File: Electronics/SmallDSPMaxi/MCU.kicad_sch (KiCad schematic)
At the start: 22 parts, among them J35 Header, SW5 TS-1187A-B-A-B, U46 STM32F030C8Tx, Y2 8MHz

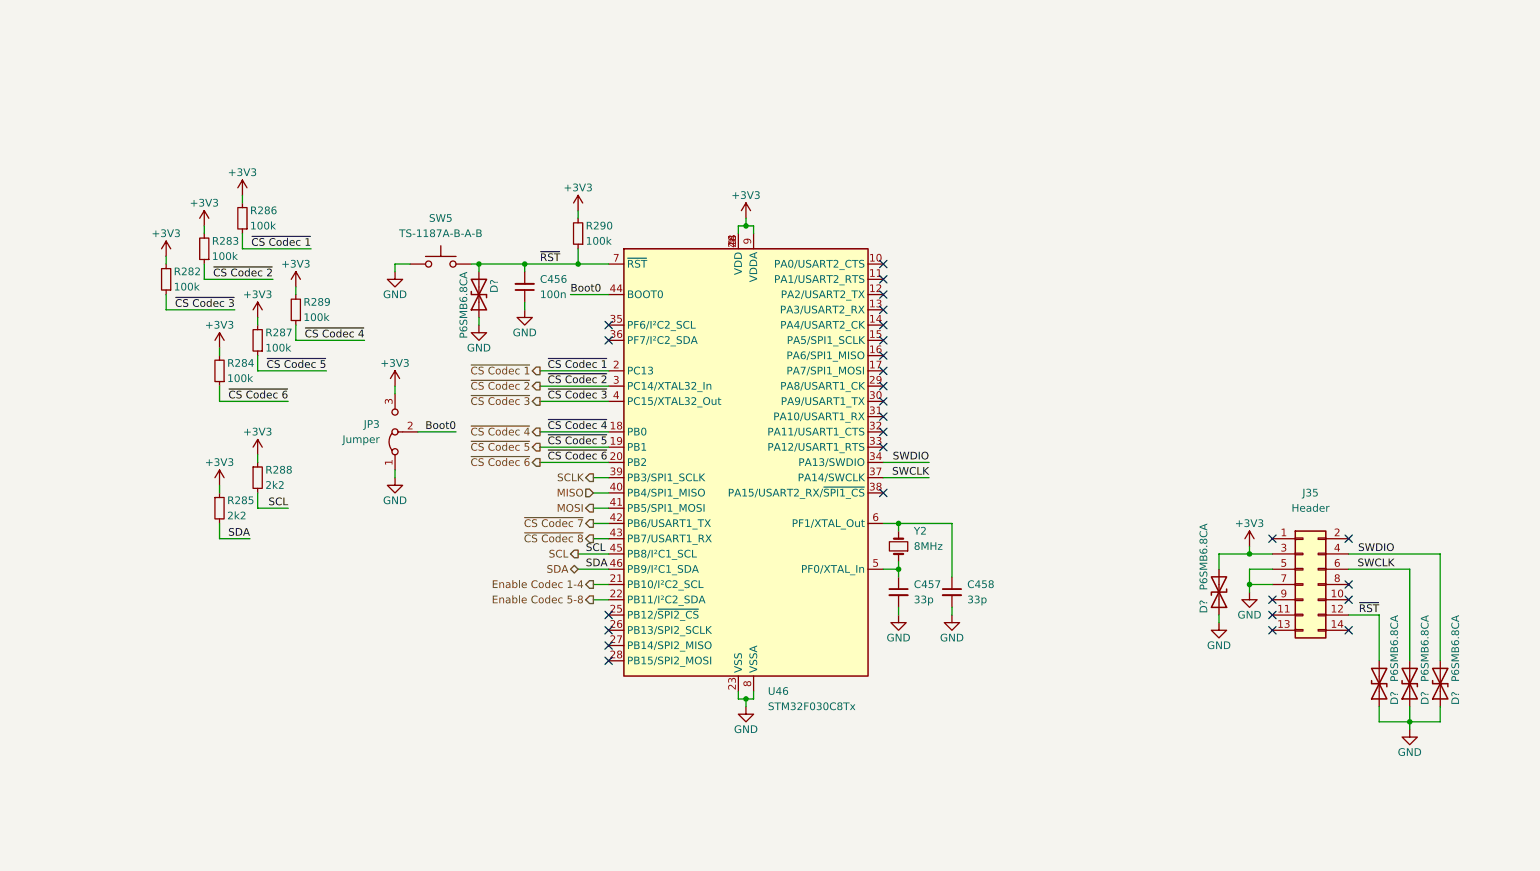
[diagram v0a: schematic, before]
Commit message: Finishes SmallDSP Maxi plus the fitting In- and Output Boards
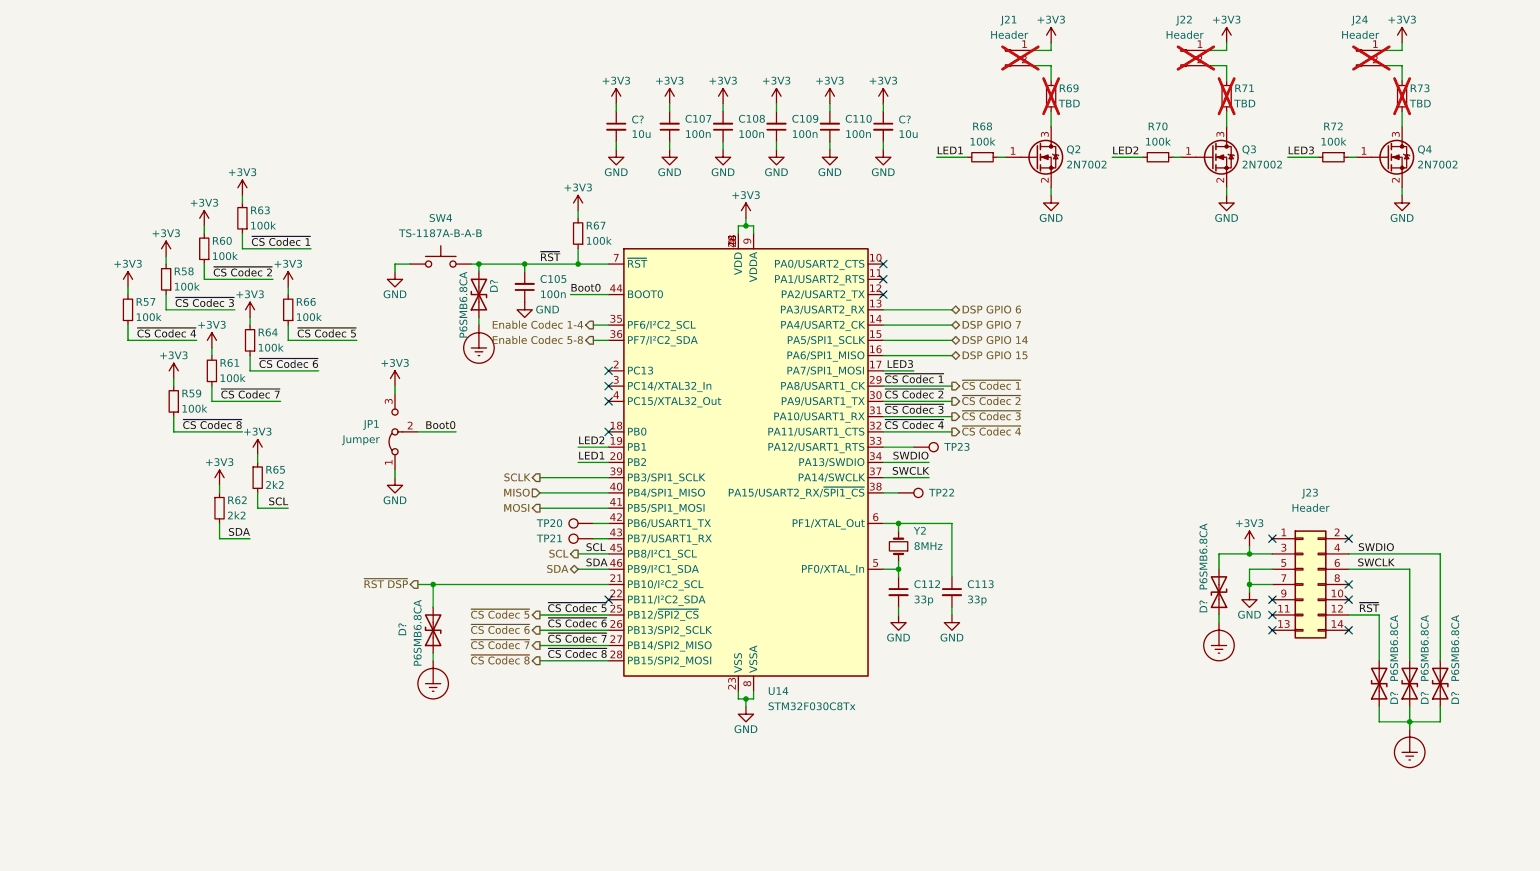
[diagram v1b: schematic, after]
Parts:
- added C107, C108, C109, C110: 100n, Capacitor_SMD:C_0402_1005Metric, symbol Device:C_Small
- added C? (x2): 10u, Capacitor_SMD:C_0603_1608Metric, symbol Device:C_Small
- added D?: P6SMB6.8CA, Diode_SMD:D_SMB, symbol Device:D_TVS
- added J21, J22, J24: Header, Connector_PinHeader_1.27mm:PinHeader_1x02_P1.27mm_Vertical, symbol Connector:Conn_01x02_Pin
- added Q2, Q3, Q4: 2N7002, Package_TO_SOT_SMD:SOT-23, symbol Device:Q_NMOS_GSD
- added R59, R61, R68, R70, R72: 100k, Resistor_SMD:R_0402_1005Metric, symbol Device:R_Small
- added R69, R71, R73: TBD, Resistor_SMD:R_0805_2012Metric_Pad1.20x1.40mm_HandSolder, symbol Device:R_Small
- added TP20, TP21, TP22, TP23: TestPoint, TestPoint:TestPoint_Pad_D1.0mm, symbol Connector:TestPoint
- C105: renamed from C456; JLC Part Number C307331 -> (none); LCSC Part # (none) -> C307331
- C112: renamed from C457; JLC Part Number C1562 -> (none); LCSC Part # (none) -> C1562
- C113: renamed from C458; JLC Part Number C1562 -> (none); LCSC Part # (none) -> C1562
- D? (x5): JLC Part Number C78395 -> (none); LCSC Part # (none) -> C78395
- J23: renamed from J35; LCSC Part # (none) -> -
- JP1: renamed from JP3; LCSC Part # (none) -> -; Manufacturer (none) -> -; Part Number (none) -> -
- R57: renamed from R289; JLC Part Number C25741 -> (none); LCSC Part # (none) -> C25741
- R58: renamed from R282; JLC Part Number C25741 -> (none); LCSC Part # (none) -> C25741
- R60: renamed from R283; JLC Part Number C25741 -> (none); LCSC Part # (none) -> C25741
- R62: renamed from R285; JLC Part Number C25879 -> (none); LCSC Part # (none) -> C25879
- R63: renamed from R286; JLC Part Number C25741 -> (none); LCSC Part # (none) -> C25741
- R64: renamed from R284; JLC Part Number C25741 -> (none); LCSC Part # (none) -> C25741
- R65: renamed from R288; JLC Part Number C25879 -> (none); LCSC Part # (none) -> C25879
- R66: renamed from R287; JLC Part Number C25741 -> (none); LCSC Part # (none) -> C25741
- R67: renamed from R290; JLC Part Number C25741 -> (none); LCSC Part # (none) -> C25741
- SW4: renamed from SW5; JLC Part Number C318884 -> (none); LCSC Part # (none) -> C318884
- U14: renamed from U46; JLC Part Number C23922 -> (none); LCSC Part # (none) -> C23922
- Y2: JLC Part Number C115962 -> (none); LCSC Part # (none) -> C115962
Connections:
- net +3V3: now also C107.2, C108.2, C109.2, C110.2, C?.1, C?.1, J21.1 (Pin_1), J22.1 (Pin_1), J24.1 (Pin_1), R59.2, R61.2
- net Enable Codec 1-4: now also U14.35 (PF6/I²C2_SCL); no longer U14.21 (PB10/I²C2_SCL)
- net Enable Codec 5-8: now also U14.36 (PF7/I²C2_SDA); no longer U14.22 (PB11/I²C2_SDA)
- net GND: now also C107.1, C108.1, C109.1, C110.1, C?.2, C?.2, Q2.2 (S), Q3.2 (S), Q4.2 (S); no longer D?.1 (A1), D?.1 (A1), D?.1 (A1), D?.1 (A1), D?.1 (A1)
- net ~{CS Codec 1}: now also U14.29 (PA8/USART1_CK); no longer U14.2 (PC13)
- net ~{CS Codec 2}: now also U14.30 (PA9/USART1_TX); no longer U14.3 (PC14/XTAL32_In)
- net ~{CS Codec 3}: now also U14.31 (PA10/USART1_RX); no longer U14.4 (PC15/XTAL32_Out)
- net ~{CS Codec 4}: now also U14.32 (PA11/USART1_CTS); no longer U14.18 (PB0)
- net ~{CS Codec 5}: now also U14.25 (PB12/~{SPI2_CS}); no longer U14.19 (PB1)
- net ~{CS Codec 6}: now also U14.26 (PB13/SPI2_SCLK); no longer U14.20 (PB2)
- net ~{CS Codec 7}: now also U14.27 (PB14/SPI2_MISO), R61.1; no longer U14.42 (PB6/USART1_TX)
- net ~{CS Codec 8}: now also U14.28 (PB15/SPI2_MOSI), R59.1; no longer U14.43 (PB7/USART1_RX)
- net DSP GPIO 6: now reaches U14.13 (PA3/USART2_RX)
- net DSP GPIO 7: now reaches U14.14 (PA4/USART2_CK)
- net DSP GPIO 14: now reaches U14.15 (PA5/SPI1_SCLK)
- net DSP GPIO 15: now reaches U14.16 (PA6/SPI1_MISO)
- net LED3: now reaches U14.17 (PA7/SPI1_MOSI)
- net LED3: now also R72.2
- net at U14.33 (PA12/USART1_RTS): now also TP23.1
- net at U14.38 (PA15/USART2_RX/~{SPI1_CS}): now also TP22.1
- new net: Q2.1 (G), R68.1
- new net: J21.2 (Pin_2), R69.1
- new net: Q3.1 (G), R70.1
- new net: TP20.1, U14.42 (PB6/USART1_TX)
- new net: TP21.1, U14.43 (PB7/USART1_RX)
- new net: J24.2 (Pin_2), R73.1
- new net: J22.2 (Pin_2), R71.1
- new net: Q4.3 (D), R73.2
- new net: Q4.1 (G), R72.1
- new net: Q2.3 (D), R69.2
- new net: Q3.3 (D), R71.2
- new net Earth_Protective: D?.1 (A1), D?.1 (A1), D?.1 (A1), D?.1 (A1), D?.1 (A1), D?.1 (A1)
- new net LED1: R68.2, U14.20 (PB2)
- new net LED2: R70.2, U14.19 (PB1)
- new net ~{RST DSP}: D?.2 (A2), U14.21 (PB10/I²C2_SCL)
- no-connect marks 28 -> 16
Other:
- moved on the sheet: R57, R64, R66

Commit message: replaces 12pin IDC out header with 14pin one because of better availability.
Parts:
- J23: footprint Connector_PinHeader_1.27mm:PinHeader_2x07_P1.27mm_Vertical_SMD -> Connector_PinHeader_1.27mm:PinHeader_2x07_P1.27mm_Vertical; Part Number 20021121-00014T4LF -> 20021111-00014T1LF

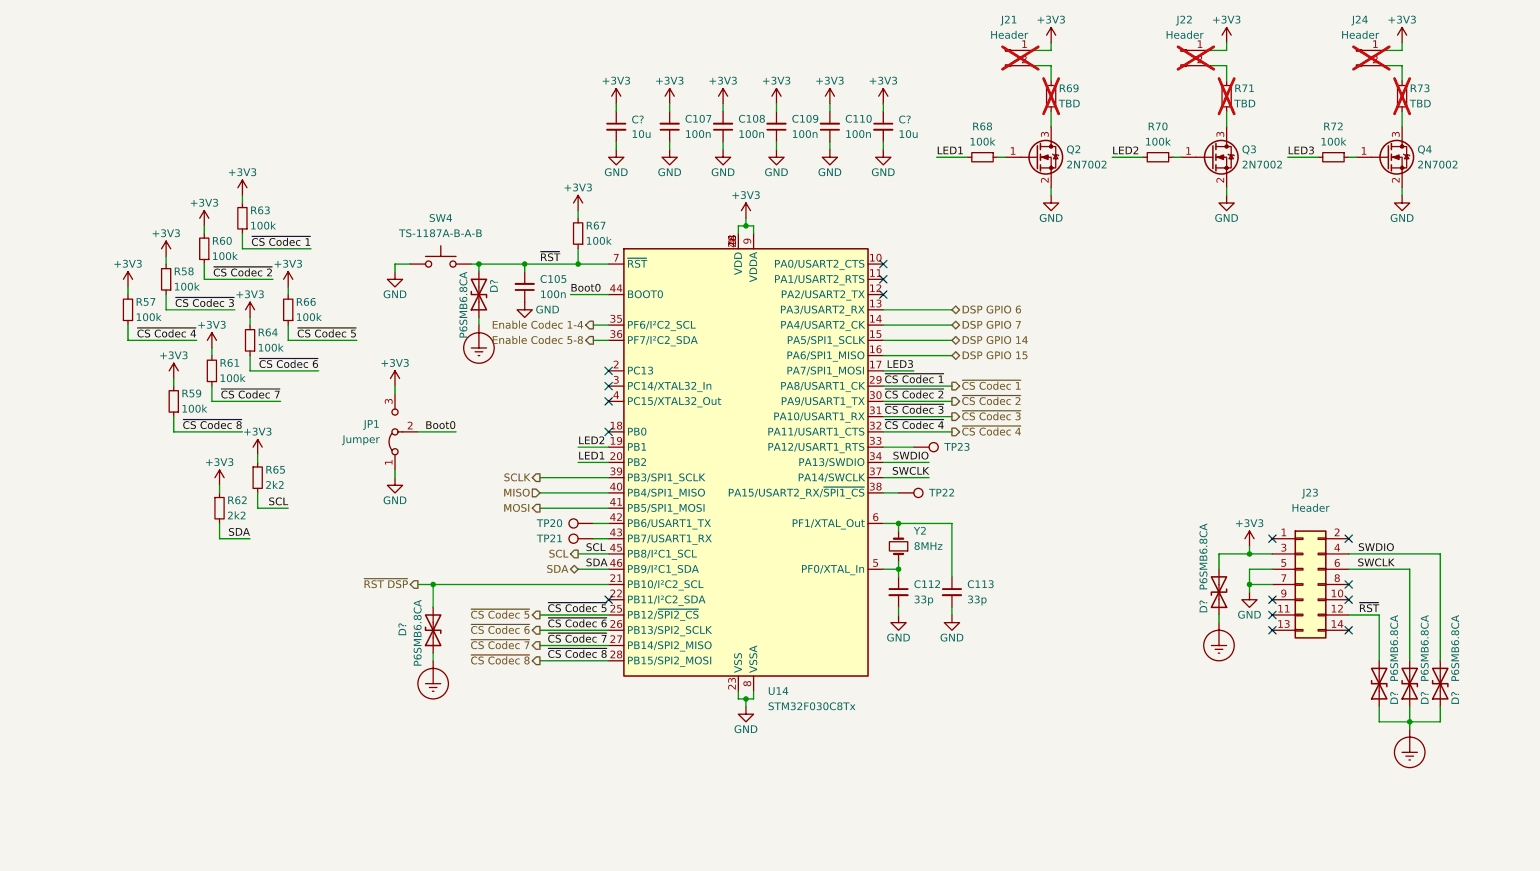
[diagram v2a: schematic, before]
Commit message: Fixes schematic mistakes, like incorrect routin of clock to codecs
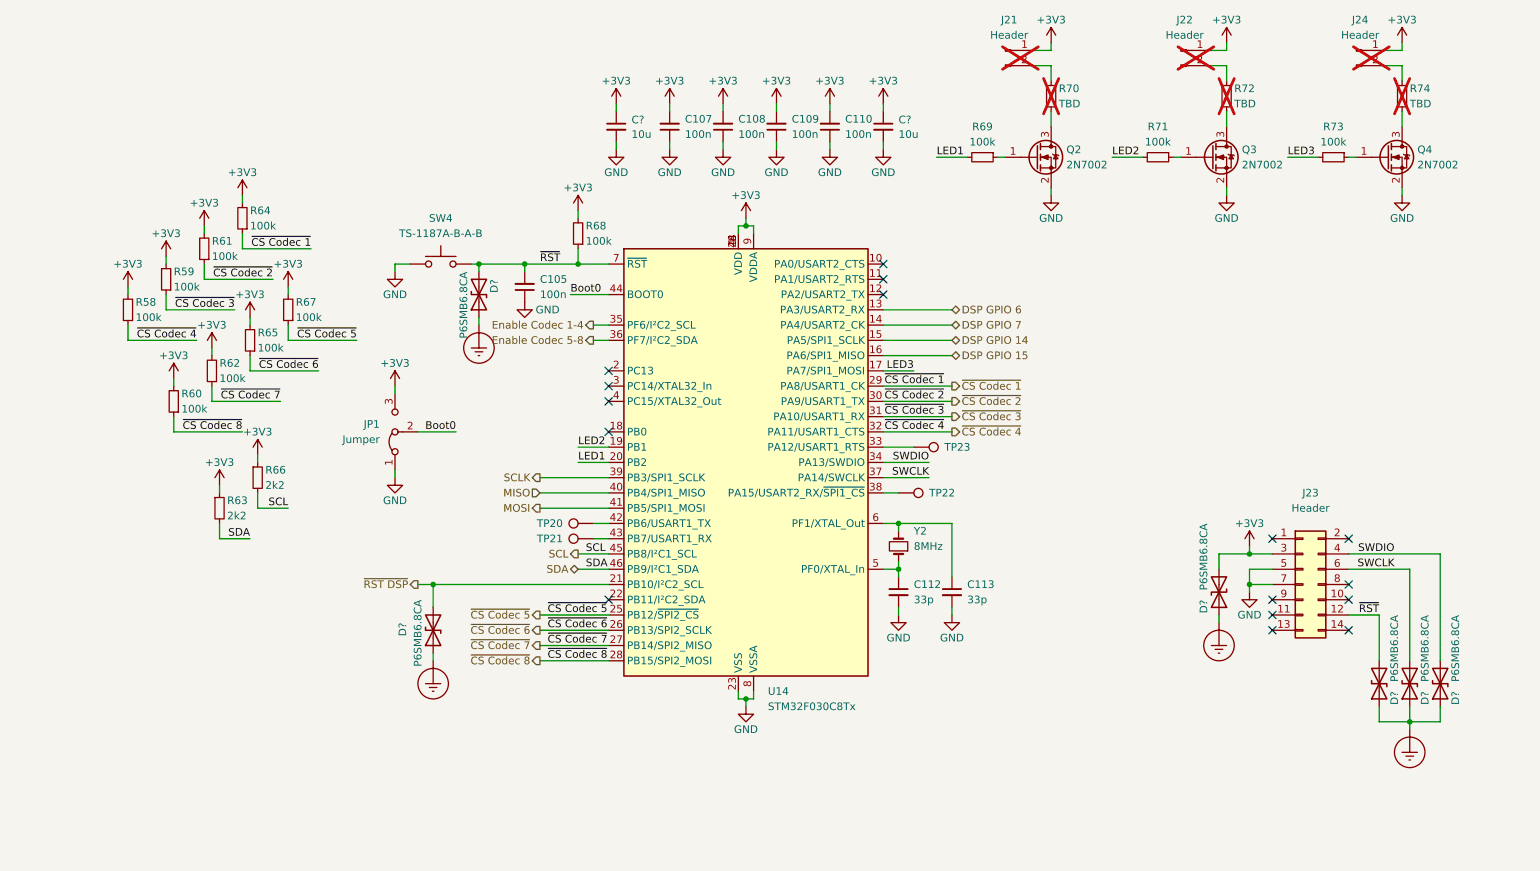
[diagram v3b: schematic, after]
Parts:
- renumbered R57 to R58, R58 to R59, R59 to R60, R60 to R61, R61 to R62, R62 to R63, R63 to R64, R64 to R65, R65 to R66, R66 to R67, R67 to R68, R68 to R69, R69 to R70, R70 to R71, R71 to R72, R72 to R73, R73 to R74

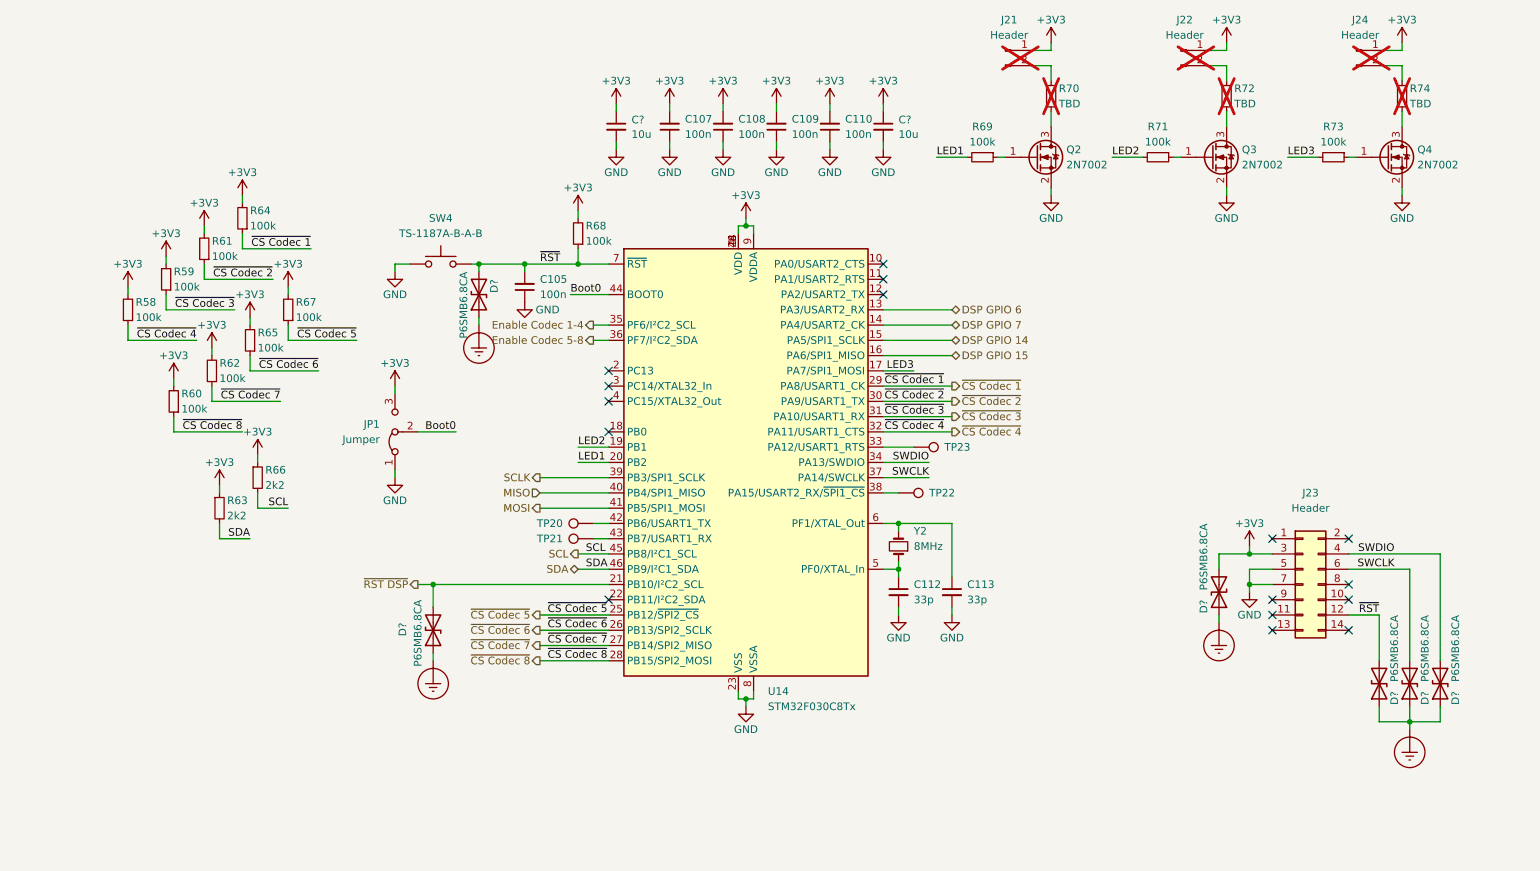
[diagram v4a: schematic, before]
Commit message: Adds clock distributer
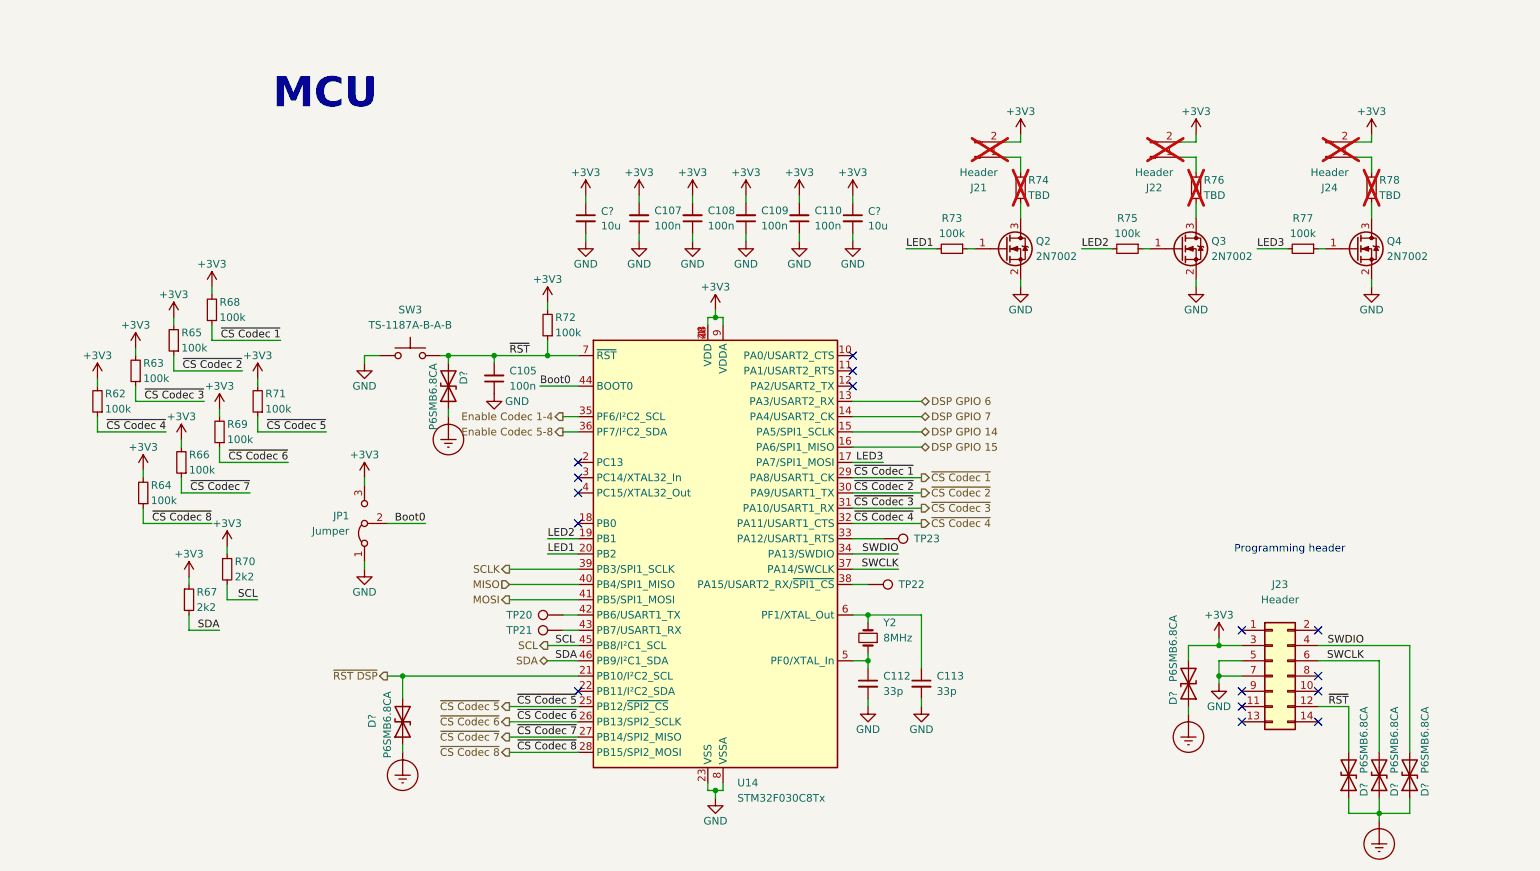
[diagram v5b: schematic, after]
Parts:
- renumbered R58 to R62, R59 to R63, R60 to R64, R61 to R65, R62 to R66, R63 to R67, R64 to R68, R65 to R69, R66 to R70, R67 to R71, R68 to R72, R69 to R73, R70 to R74, R71 to R75, R72 to R76, R73 to R77, R74 to R78, SW4 to SW3
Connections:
- net +3V3: now also J21.2 (Pin_2), J22.2 (Pin_2), J24.2 (Pin_2); no longer J21.1 (Pin_1), J22.1 (Pin_1), J24.1 (Pin_1)
- net at R74.1: now also J21.1 (Pin_1); no longer J21.2 (Pin_2)
- net at R78.1: now also J24.1 (Pin_1); no longer J24.2 (Pin_2)
- net at R76.1: now also J22.1 (Pin_1); no longer J22.2 (Pin_2)
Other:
- note added: "MCU"
- note added: "Programming header"
- company: (none) -> Till Heuer
- title: (none) -> SmallDSP Maxi
- moved on the sheet: C105, C107, C108, C109, C110, C112, C113, C?, D?, J21, J22, J23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
